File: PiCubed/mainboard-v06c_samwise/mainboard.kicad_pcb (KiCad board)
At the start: 4 copper layers, 90.2 x 95.9 mm, 190 parts, among them J1 503182-1852, J10 35362-0450, J11 MPPT board, J12 35362-0550, J13 USB_C_pycubed, J14 Conn_01x08_Horizontal, J15 35362-0550, J16 1985807, J17 35362-0450, J18 1985807, J19 35362-0650, J2 Conn_ARM_JTAG_SWD_10, J20 35362-0750, J21 35362-0750, J22 QWIIC, J3 35362-0850, J4 35362-0850, J5 35362-1250, J6 35362-0950, J7 Amphenol_901-144, J8 1985807, J9 1985807, Q10 DMP2040USS-13, Q21 DMP2040USS-13, Q5 IRLML2803, Q6 MMBT2222A-TP, Q9 IRLML2803, SW1 KMR231NG LFS, SW2 KMR231NG LFS, U16 PE014006, U17 BQ25883RGER, U2 RP2350_80QFN, U21 TPS7A4501DCQT, U23 RFM98PW, U3 MR25H40MDF, U4 ADM1176-1ARMZ-R7, U5 TPS54226PWPR, U6 LT3652HVIMSE#PBF, U7 TLV1704, Y1 ABM8-272-T3

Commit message: gerbers and picubed silkscreen version resolved
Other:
- board text added: "v06c"
- board text removed: "v06b"
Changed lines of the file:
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@@
 		)
 	)
-	(gr_text "v06b"
+	(gr_text "v06c"
 		(at 172.884473 130.154051 0)
 		(layer "F.SilkS")

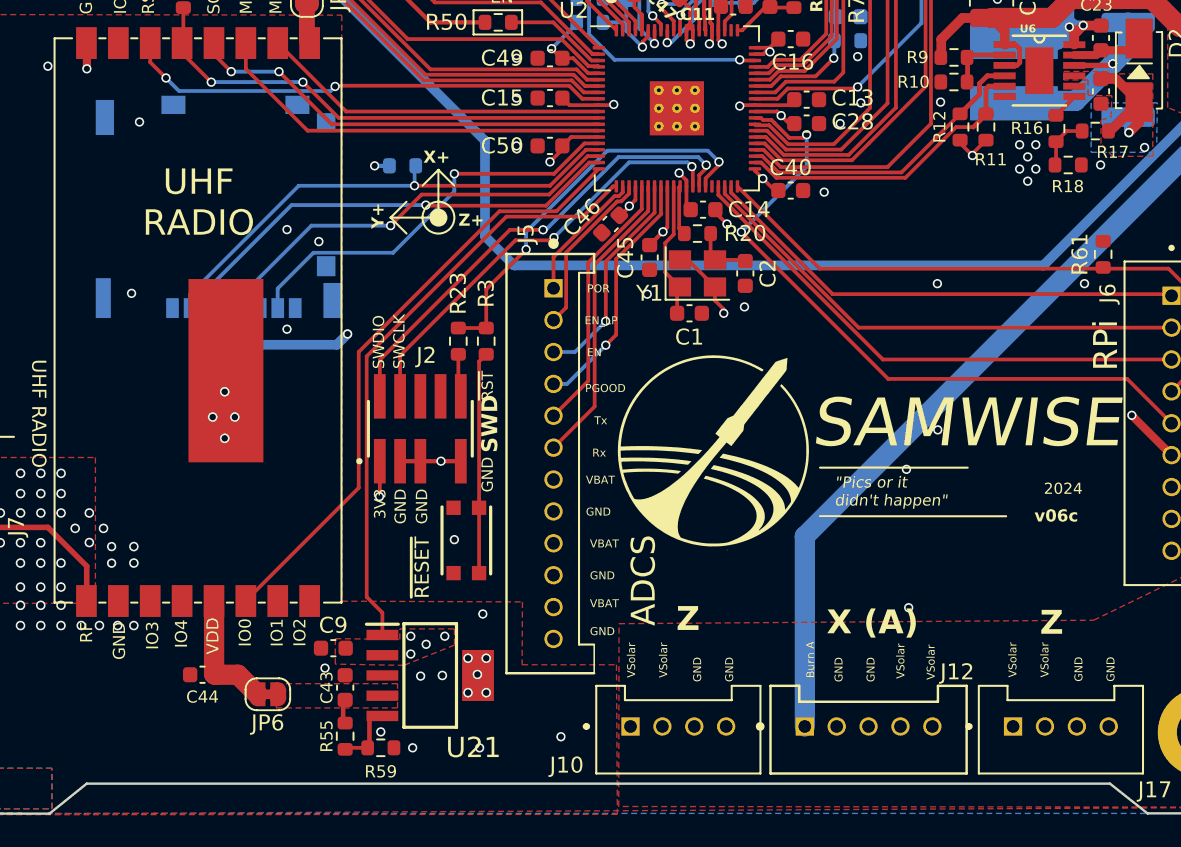
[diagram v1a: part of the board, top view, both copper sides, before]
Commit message: moved SD card
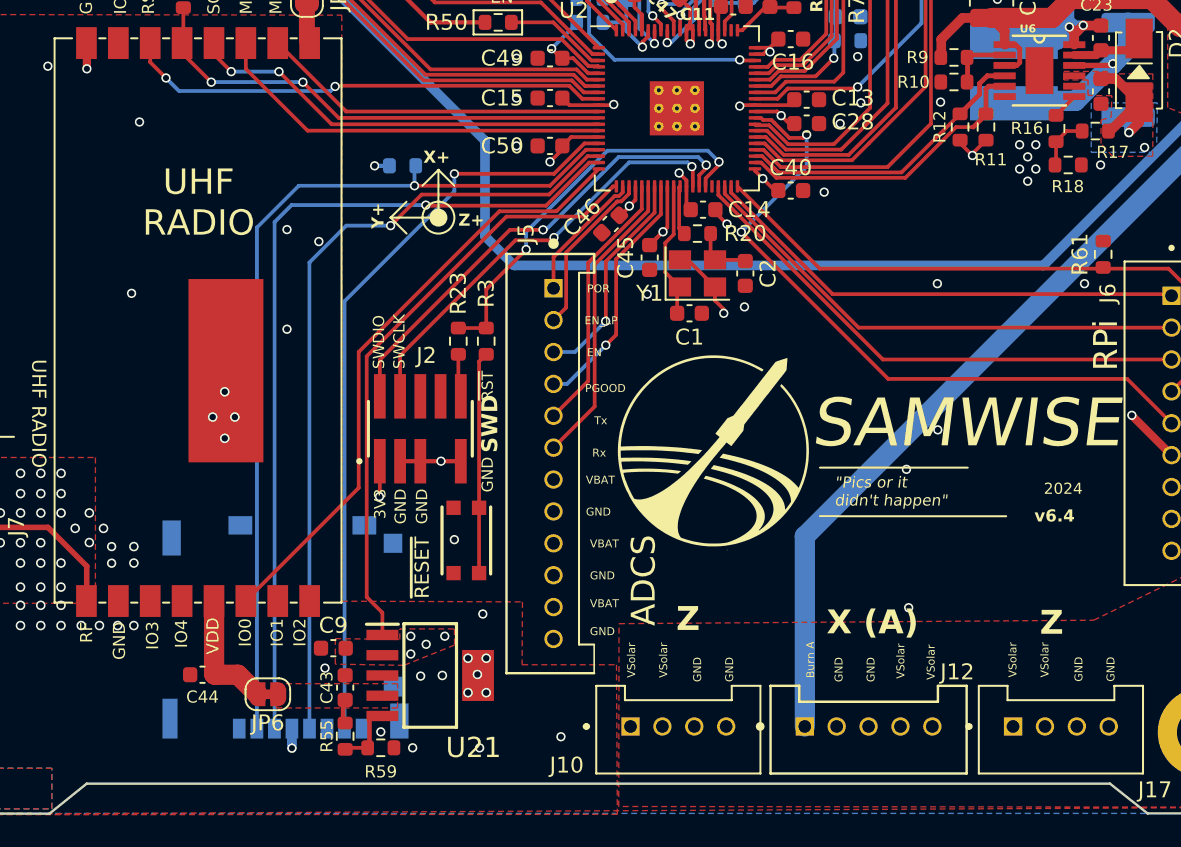
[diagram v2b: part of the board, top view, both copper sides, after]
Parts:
- moved J1 26.7 mm to (125.9, 137.3)
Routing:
- net SD_CS: track 31.5 -> 56.2 mm
- net SD_MOSI: track 29.1 -> 53.7 mm
- net SD_SCK: track 26.8 -> 50.2 mm
- net SD_MISO: track 25.8 -> 47.5 mm
- net 3.3V: track 103.5 -> 95.4 mm
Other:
- board text added: "v6.4"
- board text removed: "v06c"
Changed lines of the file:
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@@
 	(title_block
 		(title "PyCubed")
-		(date "2024-11-24")
-		(rev "06c")
+		(date "2025-03-18")
+		(rev "v6.4")
 		(company "SSI")
 	)
@@
 			(drillshape 0)
 			(scaleselection 1)
-			(outputdirectory "gerbers_v06c_20241124/")
+			(outputdirectory "gerbers_v6.4_20250318/")
 		)
 	)
@@
 	(footprint "ssi_connector:Molex_503182-1852"
 		(layer "B.Cu")
-		(at 121.7168 110.9472)
+		(at 125.91 137.325)
 		(property "Reference" "J1"
 			(at -8.027259 -7.398 -90)
@@
 		)
 	)
-	(gr_text "v06c"
+	(gr_text "v6.4"
 		(at 172.884473 130.154051 0)
 		(layer "F.SilkS")
@@
 	)
 	(via
-		(at 129.8 118.3)
-		(size 0.5842)
-		(drill 0.381)
-		(layers "F.Cu" "B.Cu")
-		(net 2)
-	)
-	(via
 		(at 169 107.1)
 		(size 0.5842)
@@
 	)
 	(via
+		(at 126.31 144.28)
+		(size 0.5842)
+		(drill 0.381)
+		(layers "F.Cu" "B.Cu")
+		(net 2)
+	)
+	(via
 		(at 156.2 88.1)
 		(size 0.5842)
@@
 	)
 	(segment
-		(start 122.1168 117.4068)
-		(end 122.1168 116.6772)
-		(width 0.6096)
-		(layer "B.Cu")
-		(net 2)
-	)
-	(segment
 		(start 158.3 88.925)
 		(end 158.375 89)
@@
 	)
 	(segment
-		(start 129.1264 118.9736)
-		(end 123.6836 118.9736)
-		(width 0.6096)
-		(layer "B.Cu")
-		(net 2)
-	)
-	(segment
-		(start 123.6836 118.9736)
-		(end 122.1168 117.4068)
-		(width 0.6096)
-		(layer "B.Cu")
-		(net 2)
-	)
-	(segment
 		(start 154.75 97.525)
 		(end 153.02 97.525)
@@
 	)
 	(segment
-		(start 129.8 118.3)
-		(end 129.1264 118.9736)
+		(start 126.31 143.055)
+		(end 126.31 144.28)
 		(width 0.6096)
 		(layer "B.Cu")
@@
 	)
 	(segment
-		(start 119.9168 115.82225)
+		(start 124.11 111.62905)
 		(end 126.73905 109)
 		(width 0.23495)
@@
 	)
 	(segment
-		(start 119.9168 116.6772)
-		(end 119.9168 115.82225)
+		(start 134 107.825)
+		(end 134.075 107.75)
 		(width 0.23495)
 		(layer "B.Cu")
@@
 	)
 	(segment
-		(start 126.73905 109)
-		(end 134 109)
+		(start 134 109)
+		(end 134 107.825)
 		(width 0.23495)
 		(layer "B.Cu")
@@
 	)
 	(segment
-		(start 134 107.825)
-		(end 134.075 107.75)
+		(start 124.11 143.055)
+		(end 124.11 111.62905)
 		(width 0.23495)
 		(layer "B.Cu")
@@
 	)
 	(segment
-		(start 134 109)
-		(end 134 107.825)
+		(start 126.73905 109)
+		(end 134 109)
 		(width 0.23495)
 		(layer "B.Cu")
@@
 	)
 	(segment
-		(start 127.53905 111.5)
-		(end 132.5 111.5)
+		(start 127.41 143.055)
+		(end 127.41 113.810648)
 		(width 0.23495)
 		(layer "B.Cu")
@@
 	)
 	(segment
-		(start 123.2168 116.6772)
-		(end 123.2168 115.82225)
+		(start 129.720648 111.5)
+		(end 132.5 111.5)
 		(width 0.23495)
 		(layer "B.Cu")
@@
 	)
 	(segment
-		(start 123.2168 115.82225)
-		(end 127.53905 111.5)
+		(start 127.41 113.810648)
+		(end 129.720648 111.5)
 		(width 0.23495)
 		(layer "B.Cu")
@@
 	)
 	(segment
-		(start 125.4168 115.44725)
-		(end 125.4168 116.6772)
+		(start 129.61 116.246316)
+		(end 129.61 143.055)
 		(width 0.23495)
 		(layer "B.Cu")
@@
 	(segment
 		(start 136.5 109.356316)
-		(end 132.651591 113.204725)
-		(width 0.23495)
-		(layer "B.Cu")
-		(net 76)
-	)
-	(segment
-		(start 127.659325 113.204725)
-		(end 125.4168 115.44725)
-		(width 0.23495)
-		(layer "B.Cu")
-		(net 76)
-	)
-	(segment
-		(start 132.651591 113.204725)
-		(end 127.659325 113.204725)
+		(end 129.61 116.246316)
 		(width 0.23495)
 		(layer "B.Cu")
@@
 	)
 	(segment
-		(start 121.0168 116.6772)
-		(end 121.0168 115.4832)
+		(start 125.22 143.045)
+		(end 125.22 111.28)
 		(width 0.23495)
 		(layer "B.Cu")
@@
 	)
 	(segment
-		(start 126.288232 110.211768)
-		(end 134.711768 110.211768)
+		(start 125.22 111.28)
+		(end 126.288232 110.211768)
 		(width 0.23495)
 		(layer "B.Cu")
@@
 	)
 	(segment
-		(start 121.0168 115.4832)
-		(end 126.288232 110.211768)
+		(start 125.21 143.055)
+		(end 125.22 143.045)
+		(width 0.23495)
+		(layer "B.Cu")
+		(net 77)
+	)
+	(segment
+		(start 126.288232 110.211768)
+		(end 134.711768 110.211768)
 		(width 0.23495)
 		(layer "B.Cu")
